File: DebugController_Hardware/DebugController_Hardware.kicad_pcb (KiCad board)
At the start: 2 copper layers, 46 parts, among them SW1 SW_Push, SW10 SW_Push, SW11 SW_Push, SW12 SW_Push, SW13 SW_Push, SW14 SW_Push, SW15 SW_Push, SW16 SW_Push, SW17 SW_Push, SW18 SW_Push, SW19 SW_Push, SW2 SW_Push, SW20 SW_Push, SW21 SW_Push, SW22 SW_Push, SW3 SW_Push, SW4 SW_Push, SW5 SW_Push, SW6 SW_Push, SW7 SW_Push, SW8 SW_Push, SW9 SW_Push, U1 TM4C129E_Launchpad

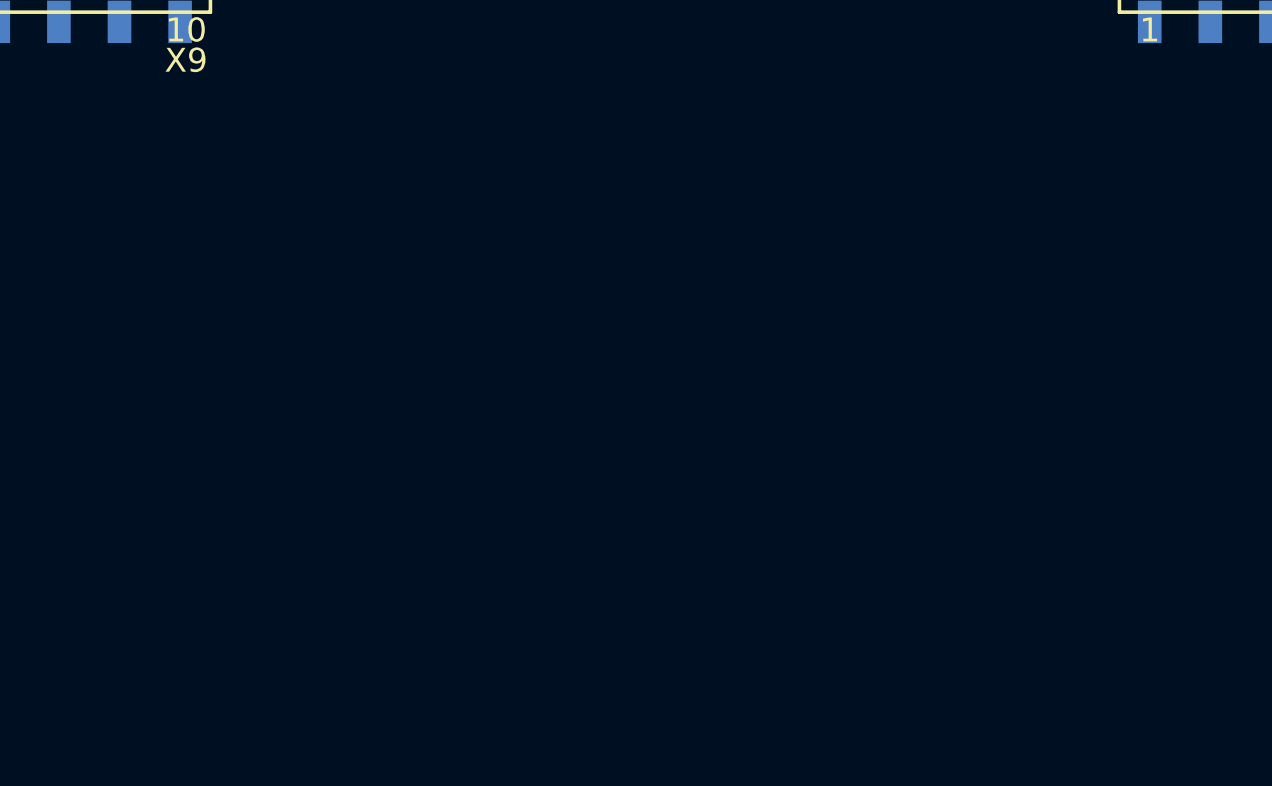
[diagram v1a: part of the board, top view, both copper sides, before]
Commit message: made changes to tiva, pot, leds
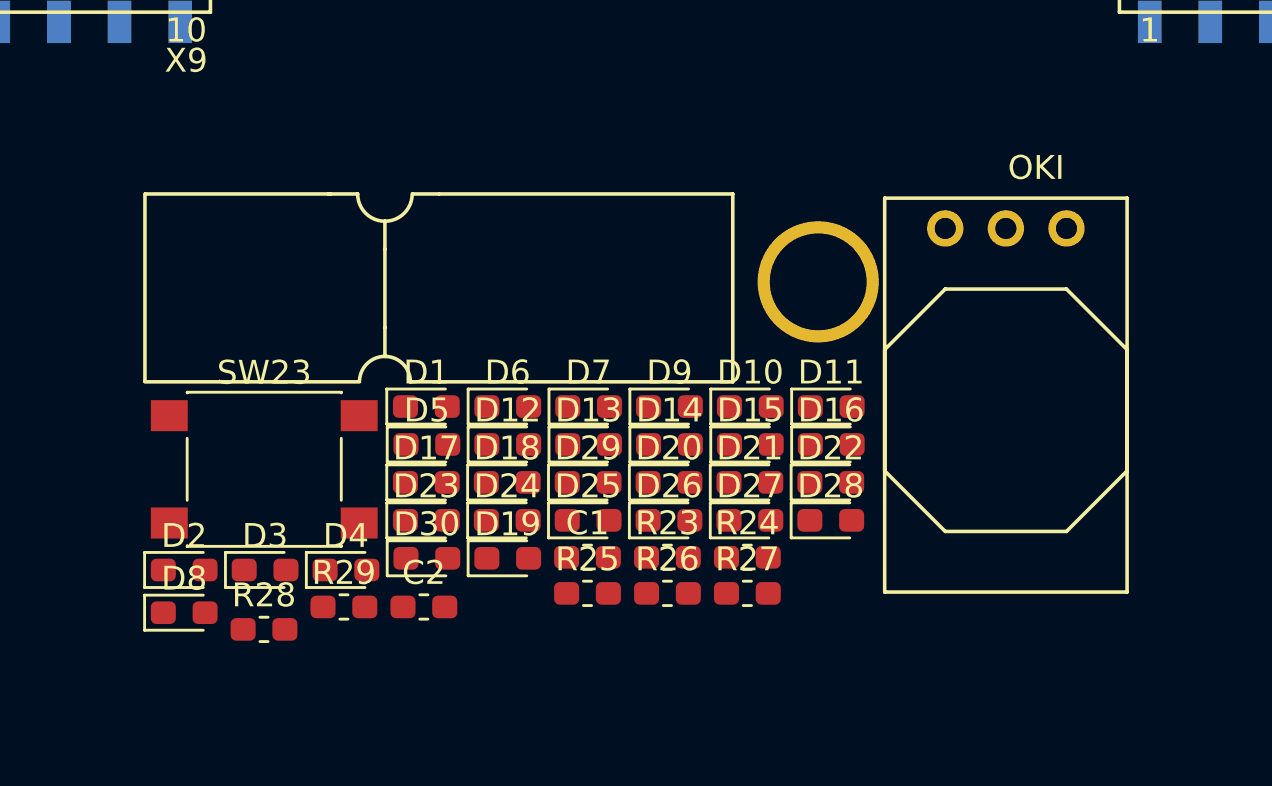
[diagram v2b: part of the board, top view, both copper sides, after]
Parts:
- added C1: 10uf, Capacitor_SMD:C_0603_1608Metric_Pad1.05x0.95mm_HandSolder, F.Cu at (56.7, 147.4)
- added C2: 10uf, Capacitor_SMD:C_0603_1608Metric_Pad1.05x0.95mm_HandSolder, F.Cu at (49.9, 149.5)
- added Conn1: AndersonPP, MRDT_Connectors:Anderson_1_Horisontal, F.Cu at (62.8, 140.0)
- added D1: LED, LED_SMD:LED_0603_1608Metric_Pad1.05x0.95mm_HandSolder, F.Cu at (50.0, 141.1)
- added D10: LED, LED_SMD:LED_0603_1608Metric_Pad1.05x0.95mm_HandSolder, F.Cu at (63.6, 141.1)
- added D11: LED, LED_SMD:LED_0603_1608Metric_Pad1.05x0.95mm_HandSolder, F.Cu at (66.9, 141.1)
- added D12: LED, LED_SMD:LED_0603_1608Metric_Pad1.05x0.95mm_HandSolder, F.Cu at (53.4, 142.7)
- added D13: LED, LED_SMD:LED_0603_1608Metric_Pad1.05x0.95mm_HandSolder, F.Cu at (56.8, 142.7)
- added D14: LED, LED_SMD:LED_0603_1608Metric_Pad1.05x0.95mm_HandSolder, F.Cu at (60.2, 142.7)
- added D15: LED, LED_SMD:LED_0603_1608Metric_Pad1.05x0.95mm_HandSolder, F.Cu at (63.6, 142.7)
- added D16: LED, LED_SMD:LED_0603_1608Metric_Pad1.05x0.95mm_HandSolder, F.Cu at (66.9, 142.7)
- added D17: LED, LED_SMD:LED_0603_1608Metric_Pad1.05x0.95mm_HandSolder, F.Cu at (50.0, 144.2)
- added D18: LED, LED_SMD:LED_0603_1608Metric_Pad1.05x0.95mm_HandSolder, F.Cu at (53.4, 144.2)
- added D19: LED, LED_SMD:LED_0603_1608Metric_Pad1.05x0.95mm_HandSolder, F.Cu at (53.4, 147.4)
- added D2: LED, LED_SMD:LED_0603_1608Metric_Pad1.05x0.95mm_HandSolder, F.Cu at (39.8, 147.9)
- added D20: LED, LED_SMD:LED_0603_1608Metric_Pad1.05x0.95mm_HandSolder, F.Cu at (60.1, 144.2)
- added D21: LED, LED_SMD:LED_0603_1608Metric_Pad1.05x0.95mm_HandSolder, F.Cu at (63.5, 144.2)
- added D22: LED, LED_SMD:LED_0603_1608Metric_Pad1.05x0.95mm_HandSolder, F.Cu at (66.9, 144.2)
- added D23: LED, LED_SMD:LED_0603_1608Metric_Pad1.05x0.95mm_HandSolder, F.Cu at (50.0, 145.8)
- added D24: LED, LED_SMD:LED_0603_1608Metric_Pad1.05x0.95mm_HandSolder, F.Cu at (53.4, 145.8)
- added D25: LED, LED_SMD:LED_0603_1608Metric_Pad1.05x0.95mm_HandSolder, F.Cu at (56.8, 145.8)
- added D26: LED, LED_SMD:LED_0603_1608Metric_Pad1.05x0.95mm_HandSolder, F.Cu at (60.1, 145.8)
- added D27: LED, LED_SMD:LED_0603_1608Metric_Pad1.05x0.95mm_HandSolder, F.Cu at (63.5, 145.8)
- added D28: LED, LED_SMD:LED_0603_1608Metric_Pad1.05x0.95mm_HandSolder, F.Cu at (66.9, 145.8)
- added D29: LED, LED_SMD:LED_0603_1608Metric_Pad1.05x0.95mm_HandSolder, F.Cu at (56.8, 144.2)
- added D3: LED, LED_SMD:LED_0603_1608Metric_Pad1.05x0.95mm_HandSolder, F.Cu at (43.2, 147.9)
- added D30: LED, LED_SMD:LED_0603_1608Metric_Pad1.05x0.95mm_HandSolder, F.Cu at (50.0, 147.4)
- added D4: LED, LED_SMD:LED_0603_1608Metric_Pad1.05x0.95mm_HandSolder, F.Cu at (46.6, 147.9)
- added D5: LED, LED_SMD:LED_0603_1608Metric_Pad1.05x0.95mm_HandSolder, F.Cu at (50.0, 142.7)
- added D6: LED, LED_SMD:LED_0603_1608Metric_Pad1.05x0.95mm_HandSolder, F.Cu at (53.4, 141.1)
- added D7: LED, LED_SMD:LED_0603_1608Metric_Pad1.05x0.95mm_HandSolder, F.Cu at (56.8, 141.1)
- added D8: LED, LED_SMD:LED_0603_1608Metric_Pad1.05x0.95mm_HandSolder, F.Cu at (39.8, 149.7)
- added D9: LED, LED_SMD:LED_0603_1608Metric_Pad1.05x0.95mm_HandSolder, F.Cu at (60.2, 141.1)
- added R23: 500, Resistor_SMD:R_0603_1608Metric_Pad1.05x0.95mm_HandSolder, F.Cu at (60.1, 147.4)
- added R24: 500, Resistor_SMD:R_0603_1608Metric_Pad1.05x0.95mm_HandSolder, F.Cu at (63.4, 147.4)
- added R25: 500, Resistor_SMD:R_0603_1608Metric_Pad1.05x0.95mm_HandSolder, F.Cu at (56.7, 148.9)
- added R26: 500, Resistor_SMD:R_0603_1608Metric_Pad1.05x0.95mm_HandSolder, F.Cu at (60.1, 148.9)
- added R27: 500, Resistor_SMD:R_0603_1608Metric_Pad1.05x0.95mm_HandSolder, F.Cu at (63.4, 148.9)
- added R28: 500, Resistor_SMD:R_0603_1608Metric_Pad1.05x0.95mm_HandSolder, F.Cu at (43.2, 150.4)
- added R29: 500, Resistor_SMD:R_0603_1608Metric_Pad1.05x0.95mm_HandSolder, F.Cu at (46.5, 149.5)
- added SW23: SW_Push, Button_Switch_SMD:SW_SPST_PTS645, F.Cu at (43.2, 143.7)
- added U2: OKI, MRDT_Devices:OKI_Horizontal, F.Cu at (69.2, 132.3)
- R1, R10, R11, R12, R13, R14, R15, R16, R17, R18, R19, R2, R20, R21, R22, R3, R4, R5, R6, R7, R8, R9: value 10K -> 500
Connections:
- R1 pad 1: Switch_Out_1 -> Drive_1
- R1 pad 2: GND -> Net-(D2-Pad2)
- R10 pad 1: Switch_Out_10 -> Arm_Ind
- R10 pad 2: GND -> Net-(D10-Pad2)
- R11 pad 1: Switch_Out_11 -> SRA_Ind
- R11 pad 2: GND -> Net-(D11-Pad2)
- R12 pad 1: Switch_Out_12 -> Arm_1
- R12 pad 2: GND -> Net-(D12-Pad2)
- R13 pad 1: Switch_Out_13 -> Arm_2
- R13 pad 2: GND -> Net-(D13-Pad2)
- R14 pad 1: Switch_Out_14 -> Arm_3
- R14 pad 2: GND -> Net-(D14-Pad2)
- R15 pad 1: Switch_Out_15 -> Arm_4
- R15 pad 2: GND -> Net-(D15-Pad2)
- R16 pad 1: Switch_Out_16 -> Other_Ind
- R16 pad 2: GND -> Net-(D16-Pad2)
- R17 pad 1: Switch_Out_17 -> Arm_5
- R17 pad 2: GND -> Net-(D17-Pad2)
- R18 pad 1: Switch_Out_18 -> Arm_6
- R18 pad 2: GND -> Net-(D18-Pad2)
- R19 pad 1: Switch_Out_19 -> Arm_7
- R19 pad 2: GND -> Net-(D19-Pad2)
- R2 pad 1: Switch_Out_2 -> Pot_Ind
- R2 pad 2: GND -> Net-(D1-Pad2)
- R20 pad 1: Switch_Out_20 -> Arm_8
- R20 pad 2: GND -> Net-(D20-Pad2)
- R21 pad 1: Switch_Out_21 -> SRA_1
- R21 pad 2: GND -> Net-(D21-Pad2)
- R22 pad 1: Switch_Out_22 -> SRA_2
- R22 pad 2: GND -> Net-(D22-Pad2)
- R3 pad 1: Switch_Out_3 -> Drive_2
- R3 pad 2: GND -> Net-(D3-Pad2)
- R4 pad 1: Switch_Out_4 -> Drive_3
- R4 pad 2: GND -> Net-(D4-Pad2)
- R5 pad 1: Switch_Out_5 -> +3V3
- R5 pad 2: GND -> Net-(D5-Pad2)
- R6 pad 1: Switch_Out_6 -> Drive_Ind
- R6 pad 2: GND -> Net-(D6-Pad2)
- R7 pad 1: Switch_Out_7 -> Drive_4
- R7 pad 2: GND -> Net-(D7-Pad2)
- R8 pad 1: Switch_Out_8 -> Drive_5
- R8 pad 2: GND -> Net-(D8-Pad2)
- R9 pad 1: Switch_Out_9 -> Drive_6
- R9 pad 2: GND -> Net-(D9-Pad2)
- RV1 pad 3: GND -> Net-(D29-Pad2)
- SW1 pad 2: Switch_Out_1 -> Drive_1
- SW10 pad 2: Switch_Out_10 -> Arm_4
- SW11 pad 2: Switch_Out_11 -> Arm_5
- SW12 pad 2: Switch_Out_12 -> Arm_6
- SW13 pad 2: Switch_Out_13 -> Arm_7
- SW14 pad 2: Switch_Out_14 -> Arm_8
- SW15 pad 2: Switch_Out_15 -> SRA_1
- SW16 pad 2: Switch_Out_16 -> SRA_2
- SW17 pad 2: Switch_Out_17 -> SRA_3
- SW18 pad 2: Switch_Out_18 -> SRA_4
- SW19 pad 2: Switch_Out_19 -> Other_1
- SW2 pad 2: Switch_Out_2 -> Drive_2
- SW20 pad 2: Switch_Out_20 -> Other_2
- SW21 pad 2: Switch_Out_21 -> Other_3
- SW22 pad 2: Switch_Out_22 -> Other_4
- SW3 pad 2: Switch_Out_3 -> Drive_3
- SW4 pad 2: Switch_Out_4 -> Drive_4
- SW5 pad 2: Switch_Out_5 -> Drive_5
- SW6 pad 2: Switch_Out_6 -> Drive_6
- SW7 pad 2: Switch_Out_7 -> Arm_1
- SW8 pad 2: Switch_Out_8 -> Arm_2
- SW9 pad 2: Switch_Out_9 -> Arm_3
- U1 pad GND: Net-(U1-PadGND) -> Other_1
- U1 pad PA5: Net-(U1-PadPA5) -> Pot_Ind
- U1 pad PA6: Net-(U1-PadPA6) -> Arm_7
- U1 pad PC4: Net-(U1-PadPC4) -> Drive_2
- U1 pad PC5: Net-(U1-PadPC5) -> Drive_3
- U1 pad PC6: Net-(U1-PadPC6) -> Drive_4
- U1 pad PC7: Net-(U1-PadPC7) -> Drive_Ind
- U1 pad PD3: Net-(U1-PadPD3) -> Drive_6
- U1 pad PD4: Net-(U1-PadPD4) -> Pot_Out
- U1 pad PD7: Net-(U1-PadPD7) -> Arm_6
- U1 pad PE0: Net-(U1-PadPE0) -> Arm_2
- U1 pad PE1: Net-(U1-PadPE1) -> Arm_3
- U1 pad PE2: Net-(U1-PadPE2) -> Arm_4
- U1 pad PE3: Net-(U1-PadPE3) -> Arm_5
- U1 pad PE4: Net-(U1-PadPE4) -> Drive_1
- U1 pad PE5: Net-(U1-PadPE5) -> Drive_5
- U1 pad PF1: Net-(U1-PadPF1) -> SRA_1
- U1 pad PF2: Net-(U1-PadPF2) -> SRA_2
- U1 pad PF3: Net-(U1-PadPF3) -> SRA_3
- U1 pad PG0: Net-(U1-PadPG0) -> SRA_4
- U1 pad PH2: Net-(U1-PadPH2) -> Other_3
- U1 pad PH3: Net-(U1-PadPH3) -> Other_4
- U1 pad PK7: Switch_Out_10 -> Net-(U1-PadPK7)
- U1 pad PL4: Net-(U1-PadPL4) -> SRA_Ind
- U1 pad PM3: Net-(U1-PadPM3) -> Other_2
- U1 pad PM4: Net-(U1-PadPM4) -> Arm_8
- U1 pad PM5: Net-(U1-PadPM5) -> Arm_Ind
- U1 pad Rese: Net-(U1-PadRese) -> Other_Ind

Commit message: attempted to organize layout
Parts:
- moved R16 186.1 mm to (137.6, 44.5)
- moved SW21 180.1 mm to (141.0, 54.6)
- moved SW19 167.0 mm to (128.3, 54.6)
- moved R11 152.5 mm to (136.3, 74.9)
- moved R10 150.9 mm to (85.1, 53.3)
- moved R17 149.0 mm to (96.9, 66.0)
- moved R21 148.4 mm to (119.4, 87.6)
- moved R12 144.2 mm to (67.7, 66.0)
- moved SW1 143.8 mm to (22.9, 73.7)
- moved R22 143.4 mm to (119.8, 97.8)
- moved SW17 142.8 mm to (139.7, 85.1)
- moved R6 142.0 mm to (31.8, 63.5)
- moved R18 141.5 mm to (96.9, 76.2)
- moved SW23 136.4 mm to (170.2, 94.0)
- moved SW4 136.0 mm to (34.3, 73.7)
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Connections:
- D5 pad 1: Net-(D5-Pad1) -> GND
- RV1 pad 3: Net-(D29-Pad2) -> GND
- U1 pad +3V3: Net-(U1-Pad+3V3) -> +3V3
- U1 pad GND: Other_1 -> GND
- U1 pad PA6: Arm_7 -> Arm_6
- U1 pad PB4: Net-(U1-PadPB4) -> Drive_Ind
- U1 pad PB5: Net-(U1-PadPB5) -> Arm_Ind
- U1 pad PC7: Drive_Ind -> Net-(U1-PadPC7)
- U1 pad PD0: Net-(U1-PadPD0) -> Other_2
- U1 pad PD1: Net-(U1-PadPD1) -> Other_1
- U1 pad PD4: Pot_Out -> Net-(U1-PadPD4)
- U1 pad PD5: Net-(U1-PadPD5) -> Pot_Out
- U1 pad PD7: Arm_6 -> Arm_5
- U1 pad PE0: Arm_2 -> Arm_1
- U1 pad PE1: Arm_3 -> Arm_2
- U1 pad PE2: Arm_4 -> Arm_3
- U1 pad PE3: Arm_5 -> Arm_4
- U1 pad PH2: Other_3 -> Net-(U1-PadPH2)
- U1 pad PH3: Other_4 -> Net-(U1-PadPH3)
- U1 pad PK0: Net-(U1-PadPK0) -> SRA_Ind
- U1 pad PK1: Net-(U1-PadPK1) -> Other_Ind
- U1 pad PL4: SRA_Ind -> Net-(U1-PadPL4)
- U1 pad PM3: Other_2 -> Net-(U1-PadPM3)
- U1 pad PM4: Arm_8 -> Arm_7
- U1 pad PM5: Arm_Ind -> Arm_8
- U1 pad PN2: Net-(U1-PadPN2) -> Other_3
- U1 pad PN3: Net-(U1-PadPN3) -> Other_4
- U1 pad Rese: Other_Ind -> Net-(U1-PadRese)
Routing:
- added copper zone on B.Cu, net +3V3
- added copper zone on F.Cu, net GND
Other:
- board text added: "ARM"
- board text added: "Arm 1"
- board text added: "Arm 2"
- board text added: "Arm 3"
- board text added: "Arm 4"
- board text added: "Arm 5"
- board text added: "Arm 6"
- board text added: "Arm 7"
- board text added: "Arm 8"
- board text added: "DRIVE"
- board text added: "Drive 1"
- board text added: "Drive 2"
- board text added: "Drive 3"
- board text added: "Drive 4"
- board text added: "Drive 5"
- board text added: "Drive 6"
- board text added: "OTHER"
- board text added: "Other 1"
- board text added: "Other 2"
- board text added: "Other 3"
- board text added: "Other 4"
- board text added: "SRA"
- board text added: "SRA 1"
- board text added: "SRA 2"
- board text added: "SRA 3"
- board text added: "SRA 4"
- board text added: "STOP"
